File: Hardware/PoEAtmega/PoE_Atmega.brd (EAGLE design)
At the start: 78.8 x 63.5 mm, 58 parts, among them IC2 ATMEGA32U4-MU, U1 ARDUINOR3-BPLACE, U2 SPX3819-3.3, U4 W5500, X1 J1011F21P, X3 microUSB, Y2 CRYSTAL-GROUNDEDSMD-3.2X2.5, Y4 8MHz

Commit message: routed but need to meet DRC
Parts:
- removed D1: MBR120, microbuilder:SOD-123
- removed R9: 100k, microbuilder:0603-MINI
- moved C6 80.9 mm to (9.45, 42.8), turned to 90 degrees
- moved U2 78.9 mm to (12.4, 42.8), turned to 180 degrees
- moved C7 72.3 mm to (15.4, 42.7)
- moved C8 69.0 mm to (17.2, 42.7)
- moved SJ1 44.2 mm to (25.5, 38.4), turned to 0 degrees
- moved C3 32.8 mm to (50.3, 33.0), turned to 0 degrees
- moved C4 32.7 mm to (50.2, 49.6), turned to 0 degrees
- moved C5 29.8 mm to (50.2, 47.6), turned to 0 degrees
- moved Y4 29.4 mm to (41.4, 27.4), turned to 90 degrees
- moved C22 28.4 mm to (20.7, 45.1), turned to 90 degrees
- moved C36 25.6 mm to (43.7, 39.9)
- moved C35 25.6 mm to (38.7, 39.9)
- moved Y2 25.5 mm to (41.2, 40.1)
- moved C21 23.8 mm to (22.8, 45.1), turned to 270 degrees
- moved C24 23.1 mm to (33.7, 39.9), turned to 270 degrees
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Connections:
- net EN: no longer R9.2, U2.3
- net GND: now also IC2.THERMAL
- net VBAT: no longer C1.2, C2.+, R6.2, U$1.V+1, U$1.V+2
- net VBUS: now also C1.2, C2.+, R6.2, U$1.V+1, U$1.V+2, U2.3; no longer R9.1
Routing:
- net GND: track 0.00 -> 233.1 mm, vias 0 -> 7
- net +3V3: track 0.00 -> 149.5 mm, vias 0 -> 7
- net VBUS: track 0.00 -> 140.7 mm, vias 0 -> 6
- net VCC-ISO: track 0.00 -> 72.7 mm, vias 0 -> 9
- net 2: track 0.00 -> 67.8 mm
- net 3: track 0.00 -> 66.2 mm, vias 0 -> 2
- net A5: track 0.00 -> 62.1 mm, vias 0 -> 2
- net VCCA: track 0.00 -> 58.0 mm, vias 0 -> 6
- net A4: track 0.00 -> 57.9 mm, vias 0 -> 2
- net A3: track 0.00 -> 54.2 mm, vias 0 -> 1
- net RST: track 0.00 -> 53.8 mm, vias 0 -> 2
- net A2: track 0.00 -> 51.9 mm, vias 0 -> 1
- net A0: track 0.00 -> 51.5 mm, vias 0 -> 1
- net A1: track 0.00 -> 50.7 mm, vias 0 -> 1
- net AREF: track 0.00 -> 47.7 mm, vias 0 -> 2
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- added copper zone on layer 1, net VBUS
- removed copper zone on layer 1, net VBAT

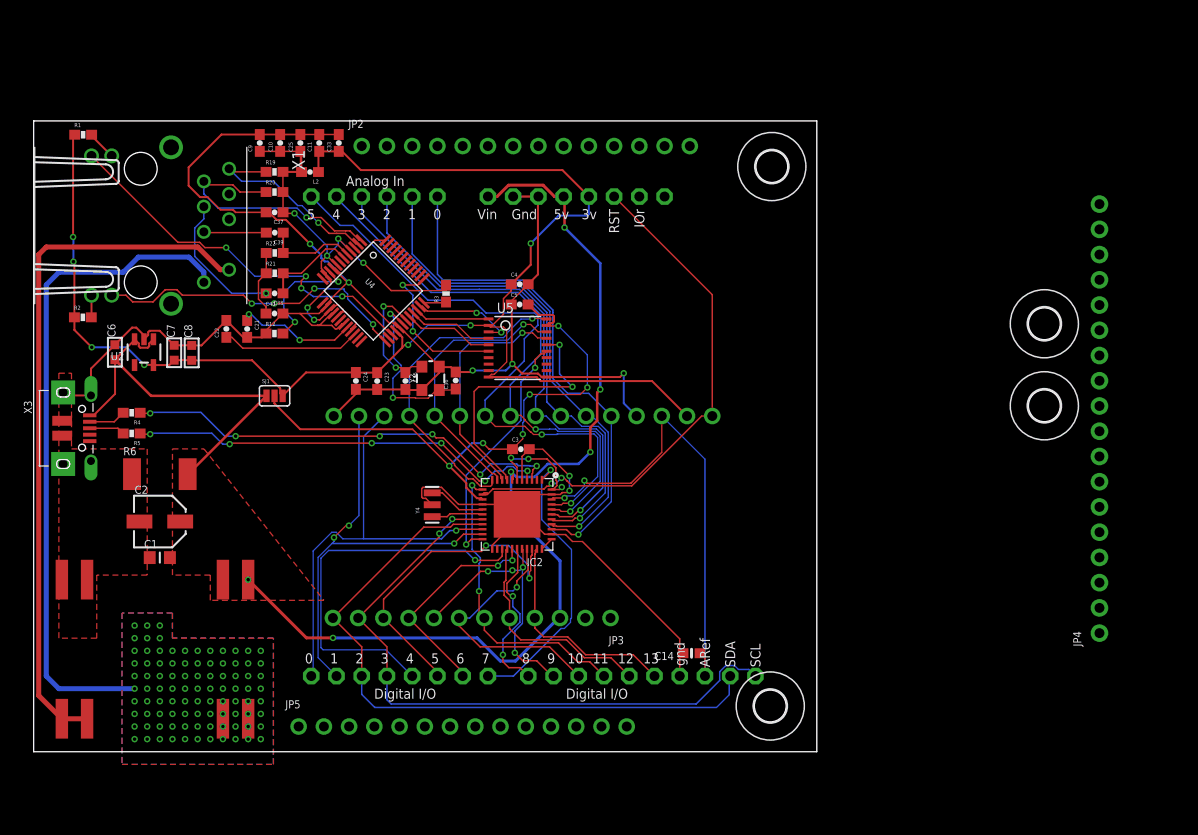
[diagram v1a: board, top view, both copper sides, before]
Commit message: HEEP-508 board for dylan review, VBUS or VISO for bottom copper fill?
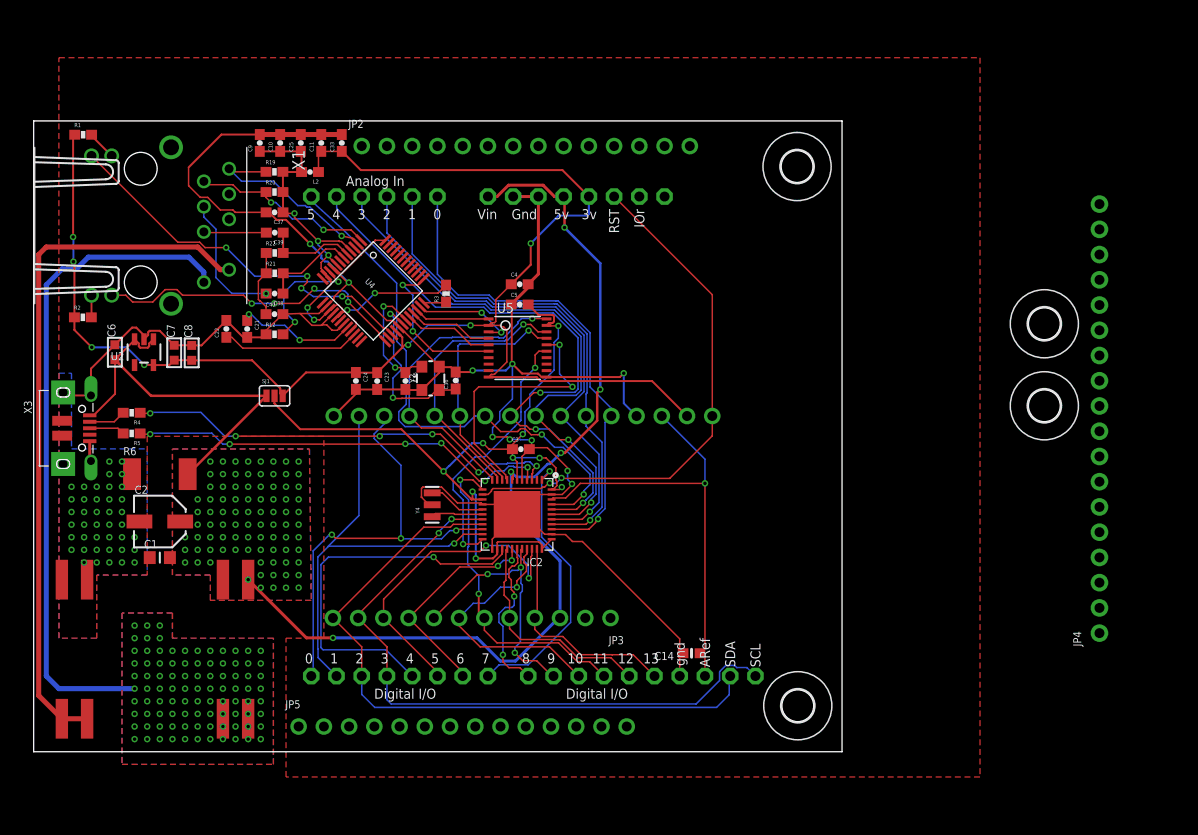
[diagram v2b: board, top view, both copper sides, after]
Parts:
- moved H4 2.77 mm to (78.2, 7.17)
- moved H3 2.54 mm to (78.1, 61.4)
- moved C33 0.30 mm to (32.3, 63.8)
- moved C11 0.20 mm to (30.2, 63.8)
- moved R12 0.08 mm to (25.5, 44.6)
- moved C40 0.06 mm to (25.5, 46.6)
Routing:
- net VCC-ISO: track 72.7 -> 83.6 mm
- net GND: track 233.1 -> 243.8 mm, vias 7 -> 51
- net TDN: track 26.4 -> 19.3 mm, vias 1 -> 2
- net A5: track 62.1 -> 55.5 mm
- net VCCA: track 58.0 -> 52.6 mm, vias 6 -> 7
- net A4: track 57.9 -> 61.6 mm, vias 2 -> 3
- net AREF: track 47.7 -> 44.5 mm, vias 2 -> 1
- net A3: track 54.2 -> 56.9 mm, vias 1 -> 2
- net 11: track 30.4 -> 32.9 mm
- net WIZ_RST: track 24.9 -> 26.9 mm
- net VBUS: track 140.7 -> 139.2 mm, vias 6 -> 92
- net SCK: track 24.3 -> 25.2 mm
- net MISO: track 32.9 -> 32.0 mm
- net RD+: track 14.1 -> 13.4 mm
- net A2: track 51.9 -> 52.6 mm
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- added copper zone on layer 16, net GND
- added copper zone on layer 16, net VBUS
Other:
- board size 78.8 x 63.5 mm -> 81.4 x 63.5 mm

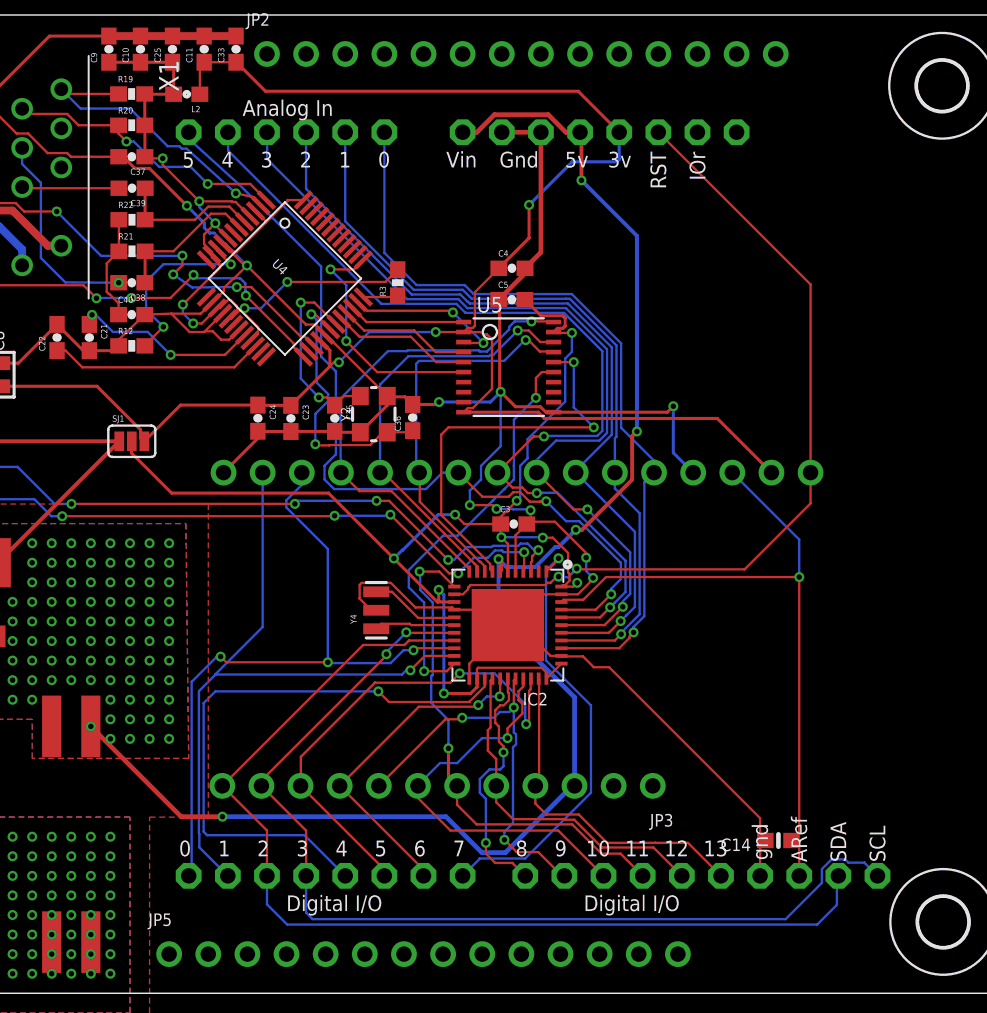
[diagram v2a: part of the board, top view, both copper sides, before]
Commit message: HEEP-508 replaced package, need to route ICSP header
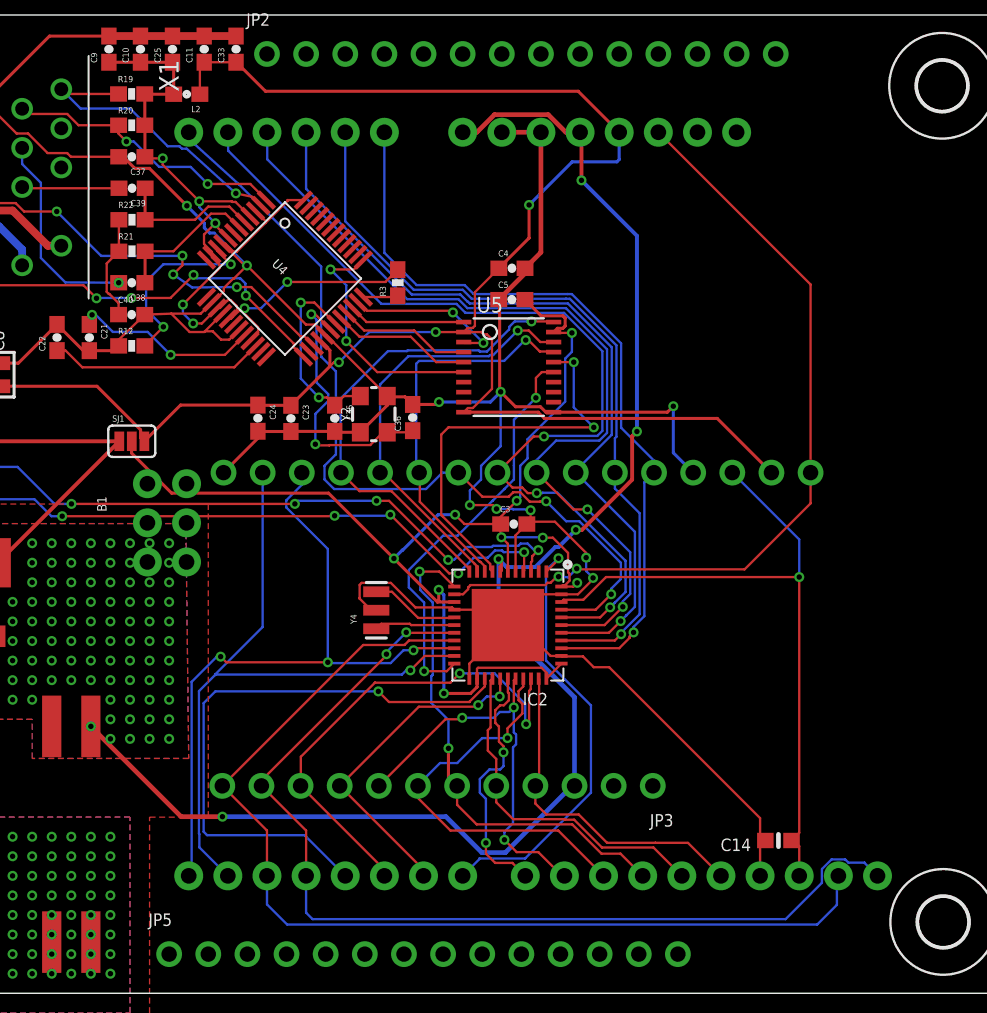
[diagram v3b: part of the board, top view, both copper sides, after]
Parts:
- removed U1: ARDUINOR3-BPLACE, adafruit:ARDUINOR3-BPLACE
- added B1: ARDUINO_UNO_R3_SHIELD_ICSP-NO_LABELS, SparkFun-Boards:UNO_R3_SHIELD_ICSP_NOLABELS
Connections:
- net +3V3: now also B1.3.3V; no longer U1.3V
- net 0: now also B1.RX; no longer U1.D0
- net 1: now also B1.TX; no longer U1.D1
- net 10: now also B1.D10; no longer U1.D10
- net 11: now also B1.D11; no longer U1.D11
- net 12: now also B1.D12; no longer U1.D12
- net 13: now also B1.D13; no longer U1.D13
- net 2: now also B1.D2, B1.SDA; no longer U1.D2, U1.SDA
- net 3: now also B1.D3, B1.SCL; no longer U1.D3, U1.SCL
- net 5: now also B1.D5; no longer U1.D5
- net 6: now also B1.D6; no longer U1.D6
- net 9: now also B1.D9; no longer U1.D9
- net A0: now also B1.A0; no longer U1.A0
- net A1: now also B1.A1; no longer U1.A1
- net A2: now also B1.A2; no longer U1.A2
- net A3: now also B1.A3; no longer U1.A3
- net A4: now also B1.A4; no longer U1.A4
- net A5: now also B1.A5; no longer U1.A5
- net AREF: now also B1.AREF; no longer U1.AREF
- net D4: now also B1.D4; no longer U1.D4
- net D7: now also B1.D7; no longer U1.D7
- net D8: now also B1.D8; no longer U1.D8
- net GND: now also B1.GND@0, B1.GND@1, B1.GND@2, B1.GND_ICSP; no longer U1.GND, U1.GND1, U1.GND2
- net MISO: now also B1.MISO
- net MOSI: now also B1.MOSI
- net RST: now also B1.RES, B1.RST_ICSP; no longer U1.RESET
- net SCK: now also B1.SCK
- net VBUS: now also B1.5V, B1.5V_ICSP, B1.VIN; no longer U1.5V, U1.VIN

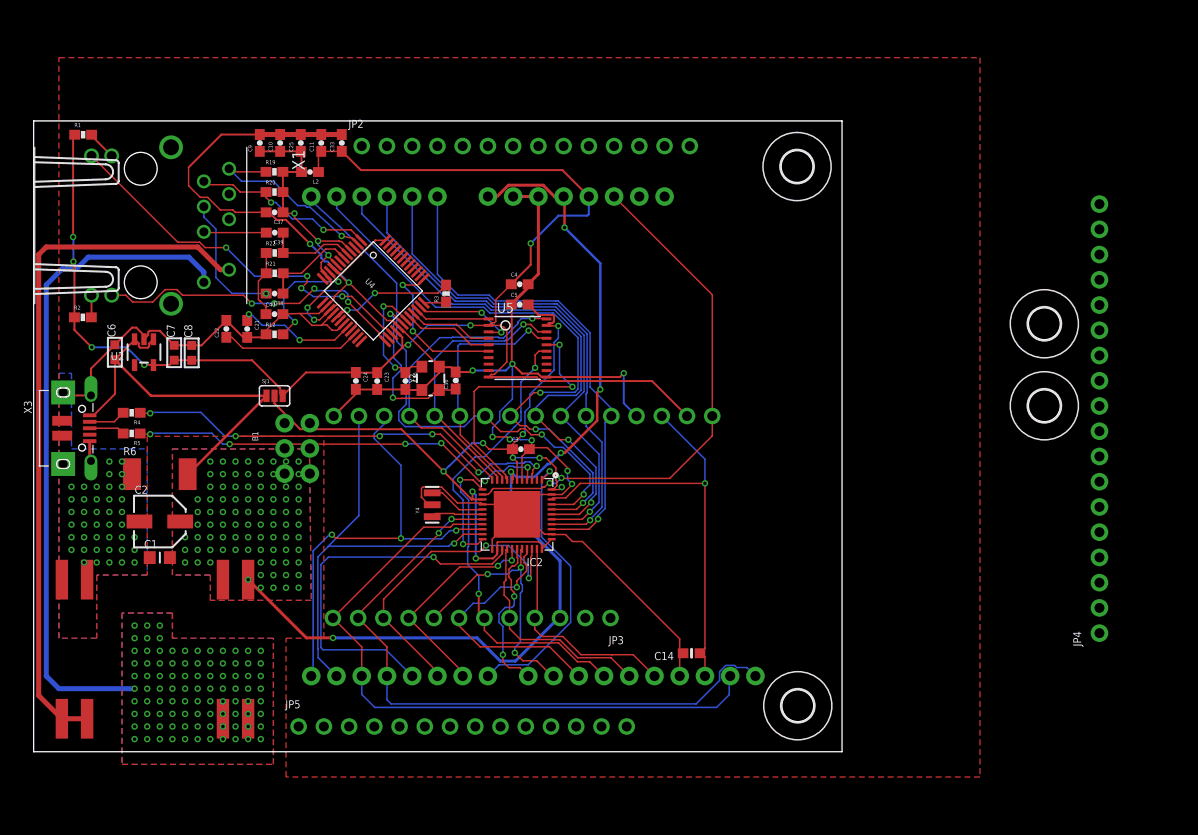
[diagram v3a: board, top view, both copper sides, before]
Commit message: HEEP-508 routed ICSP headers
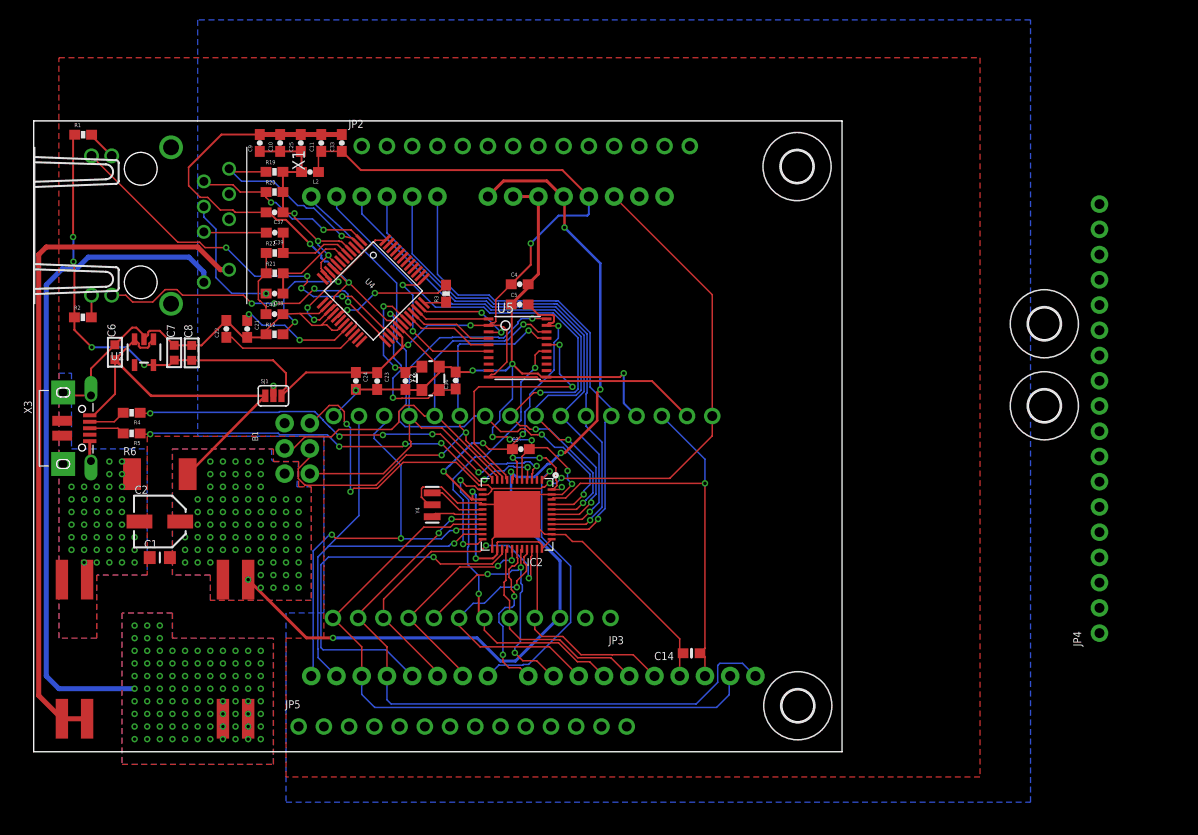
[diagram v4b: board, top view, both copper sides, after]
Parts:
- moved SJ1 0.12 mm to (25.4, 38.4)
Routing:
- net RST: track 53.9 -> 83.3 mm, vias 2 -> 4
- net SCK: track 25.2 -> 48.1 mm, vias 1 -> 3
- net VCC-ISO: track 83.6 -> 64.1 mm, vias 9 -> 10
- net MOSI: track 27.9 -> 45.9 mm
- net MISO: track 32.0 -> 46.4 mm
- net +3V3: track 149.5 -> 151.3 mm
- net 3: track 66.2 -> 66.9 mm
- net GND: track 243.8 -> 244.1 mm, vias 51 -> 52
- net VBUS: track 139.2 -> 139.5 mm, vias 92 -> 83
- added copper zone on layer 16, net VCC-ISO

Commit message: HEEP-508 rdy for dylan review
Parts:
- removed JP2, JP5: (no value), microbuilder:1X14_ROUND70
- removed JP4: (no value), microbuilder:1X18_ROUND70
- added J1, J2, J5, J6: (no value), SparkFun-Connectors:1X18
- added J3, J4: (no value), SparkFun-Connectors:1X10
- moved H2 97.7 mm to (11.6, 2.80)
- moved H3 72.6 mm to (5.71, 67.0)
- moved H1 30.4 mm to (81.4, 67.0)
- moved C33 12.5 mm to (20.5, 68.1), turned to 270 degrees
- moved L2 8.97 mm to (25.5, 69.1), turned to 0 degrees
- moved C11 8.76 mm to (22.6, 68.1), turned to 270 degrees
- moved R1 6.04 mm to (12.2, 65.7)
- moved H4 5.05 mm to (80.7, 2.80)
- moved C25 4.17 mm to (25.5, 67.0), turned to 180 degrees
- moved C9 1.71 mm to (25.5, 62.9), turned to 180 degrees
- moved C10 1.31 mm to (25.5, 65.0), turned to 180 degrees
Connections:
- net 0: now also J5.1, J6.1
- net 1: now also J5.3, J6.3
- net 10: now also J3.3, J4.3
- net 11: now also J3.5, J4.5
- net 12: now also J3.7, J4.7
- net 13: now also J3.9, J4.9
- net 2: now also J5.5, J6.5
- net 3: now also J5.7, J6.7
- net 5: now also J5.11, J6.11
- net 6: now also J5.13, J6.13
- net 9: now also J3.1, J4.1
- net A0: now also J1.17, J2.17
- net A1: now also J1.14, J2.14
- net A2: now also J1.11, J2.11
- net A3: now also J1.8, J2.8
- net A4: now also J1.5, J2.5
- net A5: now also J1.2, J2.2
- net D4: now also J5.9, J6.9
- net D7: now also J5.15, J6.15
- net D8: now also J5.17, J6.17
- net GND: now also J1.12, J1.15, J1.18, J1.3, J1.6, J1.9, J2.12, J2.15, J2.18, J2.3, J2.6, J2.9, J3.10, J3.2, J3.4, J3.6, J3.8, J4.10, J4.2, J4.4, J4.6, J4.8, J5.10, J5.12, J5.14, J5.16, J5.18, J5.2, J5.4, J5.6, J5.8, J6.10, J6.12, J6.14, J6.16, J6.18, J6.2, J6.4, J6.6, J6.8
- net VCC-ISO: now also J1.1, J1.10, J1.13, J1.16, J1.4, J1.7, J2.1, J2.10, J2.13, J2.16, J2.4, J2.7
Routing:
- net 13: track 22.2 -> 67.2 mm, vias 0 -> 2
- net 9: track 26.6 -> 68.1 mm
- net 10: track 26.5 -> 67.8 mm
- net 12: track 22.4 -> 62.3 mm, vias 0 -> 1
- net A0: track 51.0 -> 88.9 mm
- net 11: track 32.8 -> 70.2 mm
- net A1: track 50.7 -> 83.6 mm
- net GND: track 244.1 -> 211.4 mm
- net A2: track 52.6 -> 80.2 mm
- net D8: track 16.5 -> 41.4 mm
- net D7: track 28.7 -> 52.6 mm
- net +3V3: track 151.3 -> 174.9 mm
- net A3: track 56.9 -> 79.7 mm
- net 6: track 22.1 -> 43.4 mm
- net 5: track 32.1 -> 50.9 mm
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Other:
- board size 81.4 x 63.5 mm -> 85.2 x 72.4 mm
- board text added: "+"
- board text added: "0"
- board text added: "1"
- board text added: "10"
- board text added: "11"
- board text added: "12"
- board text added: "13"
- board text added: "2"
- board text added: "3"
- board text added: "4"
- board text added: "5"
- board text added: "6"
- board text added: "7"
- board text added: "8"
- board text added: "9"
- board text added: "A0"
- board text added: "A1"
- board text added: "A2"
- board text added: "A3"
- board text added: "A4"
- board text added: "A5"
